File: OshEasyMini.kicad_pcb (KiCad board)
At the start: 6 copper layers, 17.2 x 35.4 mm, 119 parts, among them J1 TAGCONNECT, J10 Conn_01x04_MountingPin, J3 SMA_Edgelaunch, J4 Screw_Terminal_01x03, J5 UFL, J6 Conn_01x02, Q1 SiA449DJ, Q2 AO3400A, Q3 SiA449DJ, U1 MIA-M10Q, U11 CPT-7502-65-SMT-TR, U12 LM293QT, U17 MCP73831-2-OT, U18 TC2185-3.3VxCTTR, U19 W25Q64JVXGIQ, U2 WE-TVS-82400102, U20 SISB46DN, U21 SN74LVC1G80QDCKTQ1, U3 ADXL375, U4 MS5607-02BA, U6 MCP130-xxxxTT, U7 DRV5012AEDMRR, U8 CC1200, U9 ATSAMD21G17D-A, X2 ECS-160-8-36Q-AES-TR1, Y1 40mhz 8pF 30 Ohms, Y2 32.768khz

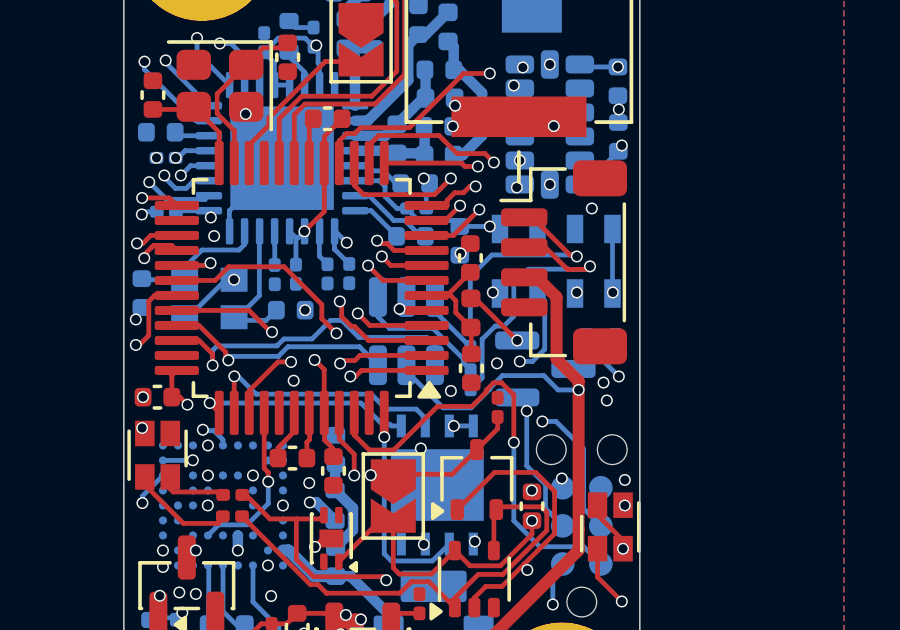
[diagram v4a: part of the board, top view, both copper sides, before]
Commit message: ready for final prod after silkscreens
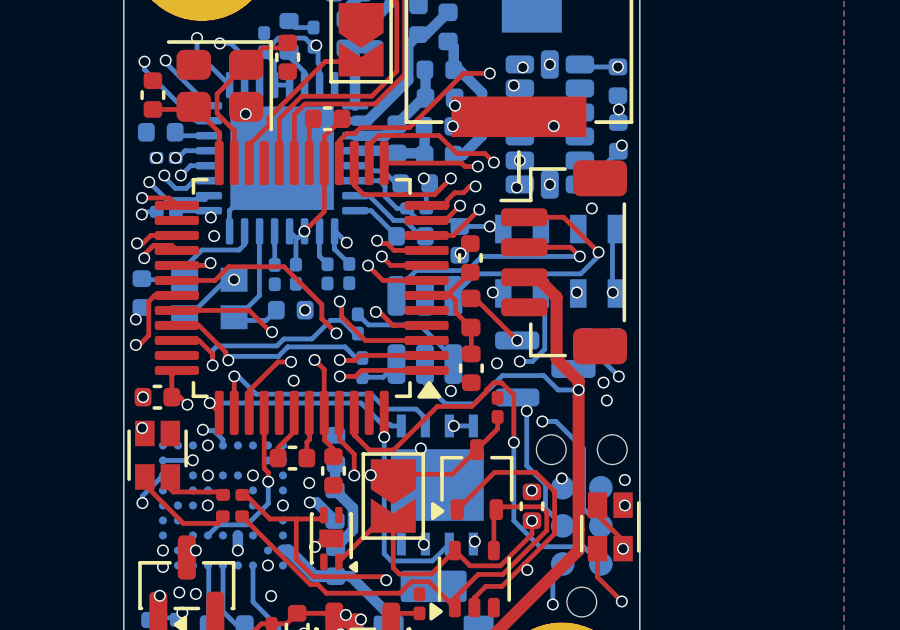
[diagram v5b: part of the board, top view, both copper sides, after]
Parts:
- J4: value Screw_Terminal_01x03 -> PYROS
- J6: value Conn_01x02 -> BAT
- JP1: value SolderJumper_2_Open -> MAG BYPASS
- JP2: value SolderJumper_2_Open -> BOOT
- R1, R9: value 22 -> 33
- moved R1 3.78 mm to (97.8, 45.0)
- moved R9 3.63 mm to (98.0, 46.5)
- moved U2 0.62 mm to (100.0, 45.2)
- moved U4 0.11 mm to (104.5, 43.0)
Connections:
- R1 pad 1: Net-(J10-Pin_1) -> Net-(R1-Pad1)
- R1 pad 2: Net-(R1-Pad2) -> /USB_D+
- R9 pad 1: Net-(J10-Pin_2) -> Net-(R9-Pad1)
- R9 pad 2: Net-(R9-Pad2) -> /USB_D-
- U2 pad 1: Net-(R9-Pad2) -> Net-(J10-Pin_2)
- U2 pad 3: Net-(R1-Pad2) -> Net-(J10-Pin_1)
- U2 pad 4: /USB_D+ -> Net-(R1-Pad1)
- U2 pad 6: /USB_D- -> Net-(R9-Pad1)
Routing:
- net Net-(R9-Pad2): track 4.57 -> 0.00 mm
- net Net-(R1-Pad1): track 0.00 -> 3.98 mm
- net /USB_D+: track 11.1 -> 7.69 mm
- net Net-(R1-Pad2): track 2.15 -> 0.00 mm
- net Net-(R9-Pad1): track 0.00 -> 1.32 mm
- net /AC_INT1: track 17.8 -> 16.6 mm
- net Net-(J10-Pin_1): track 7.94 -> 8.83 mm
- net /USB_D-: track 7.79 -> 7.18 mm
- net GND: vias 52 -> 51

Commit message: added silks
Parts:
- added J3: SMA_Edgelaunch, Connector_Coaxial:SMA_Amphenol_132289_EdgeMount, B.Cu at (106.0, 32.8)
- moved J3 0.40 mm to (103.2, 32.8)
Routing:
- net /BUZZ: track 19.4 -> 22.4 mm
- net GND: track 15.2 -> 17.1 mm, vias 51 -> 58
- net /AC_INT1: track 16.6 -> 17.6 mm
- net /AC_INT2: track 19.7 -> 20.2 mm
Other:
- board text added: "-"
- board text added: "C0"
- board text added: "GPS"
- board text added: "L1"
- board text added: "MG"
- board text added: "MetrumITX v1.0 433M"
- board text added: "USB"

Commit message: v1 sent for build
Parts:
- moved U7 0.40 mm to (96.5, 52.2)
- moved J3 0.30 mm to (106.3, 32.8)
- moved D2 0.07 mm to (101.8, 50.2)
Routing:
- net GND: track 17.1 -> 16.9 mm, vias 58 -> 59
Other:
- board text added: "ANT^"
- board text added: "PPS"

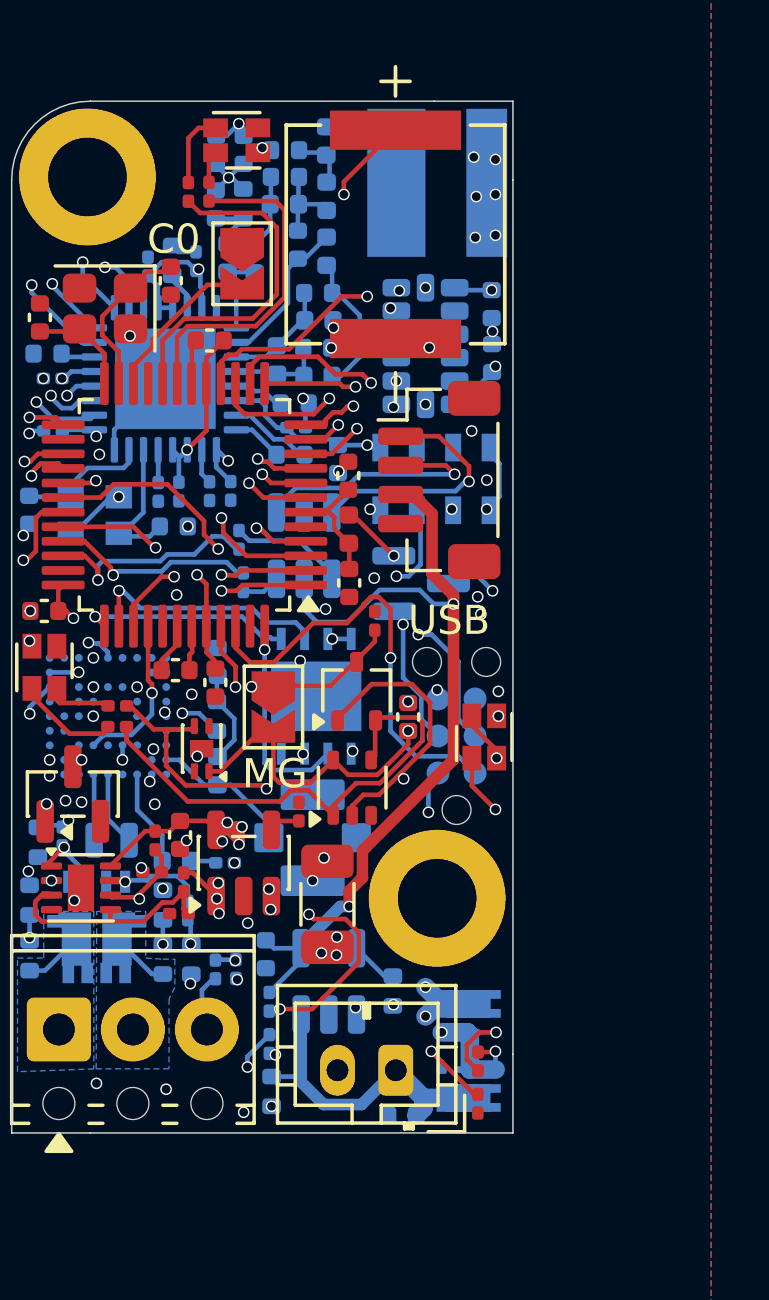
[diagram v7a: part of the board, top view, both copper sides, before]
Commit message: v1.1 revision with capacitor moved to ease in assembly, and added copyright per TAPR
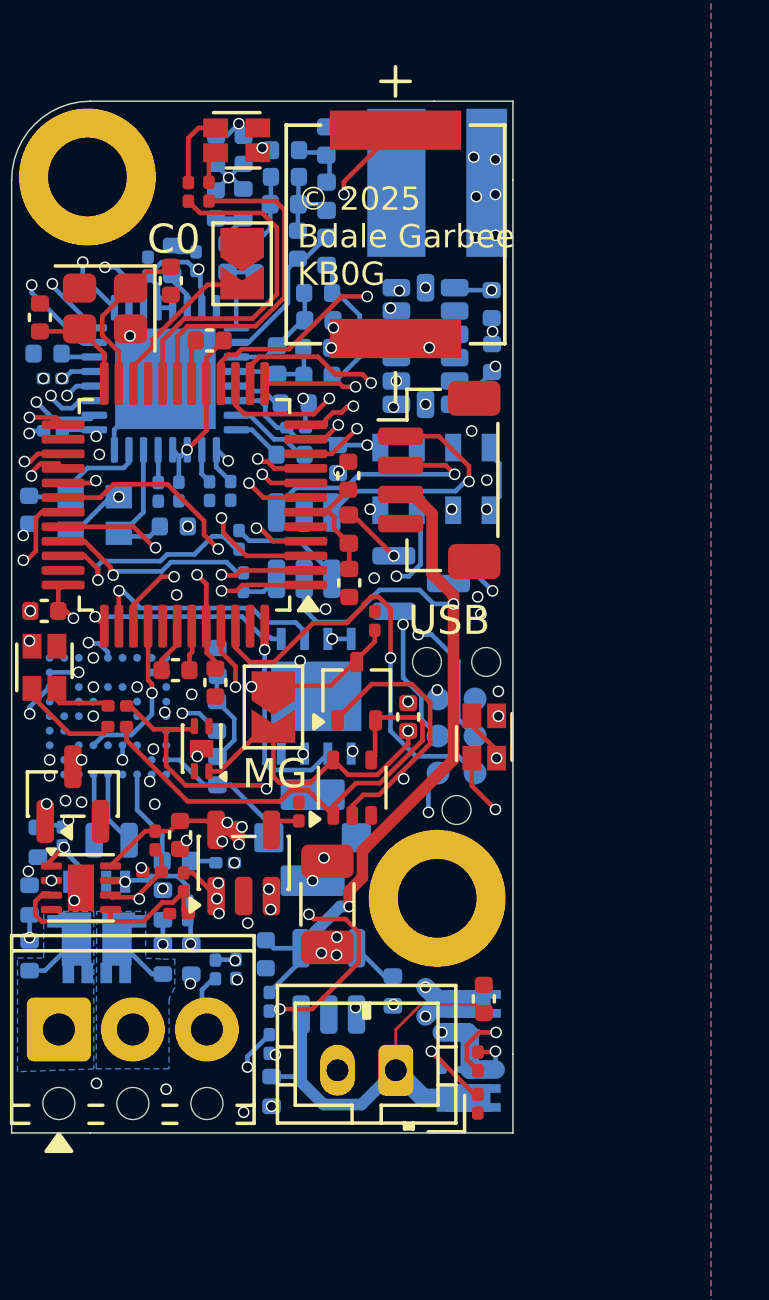
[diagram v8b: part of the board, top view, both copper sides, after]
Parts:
- C21: moved to F.Cu
- moved C21 4.88 mm to (106.2, 60.8), turned to -90 degrees
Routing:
- net V_CHARGE: track 11.0 -> 15.1 mm
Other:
- board text added: "MetrumITX v1.1 433M"
- board text added: "© 2025 Bdale Garbee KB0G"
- board text removed: "MetrumITX v1.0 433M"
